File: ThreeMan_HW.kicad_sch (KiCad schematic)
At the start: 76 parts, among them J1 USB4135-GF-A, J2 JST-PH-2mm, J3 TC2030_ICSP, SW1 SW_Push, SW2 SW_SPDT_312, U1 MCP73831T-2ACI/OT, U2 74HC595, U3 ATTINY85-20SUR, U4 TPS7A20, U5 ULQ2003D, U6 ULQ2003D

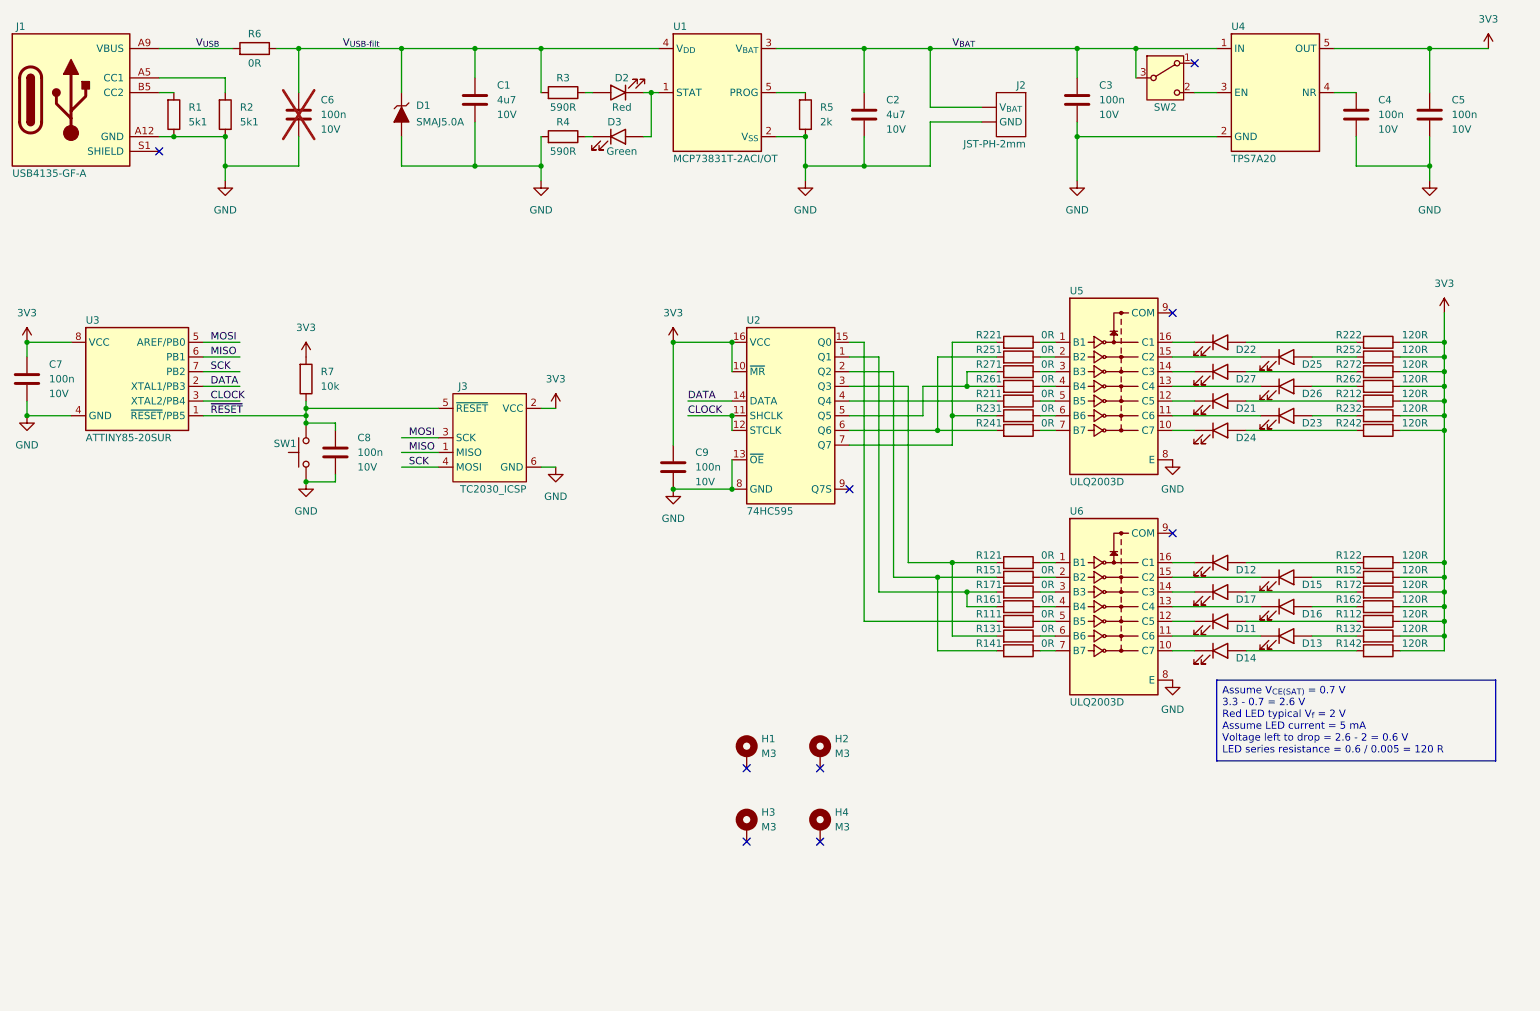
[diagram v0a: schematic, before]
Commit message: Ported all components to zpklib
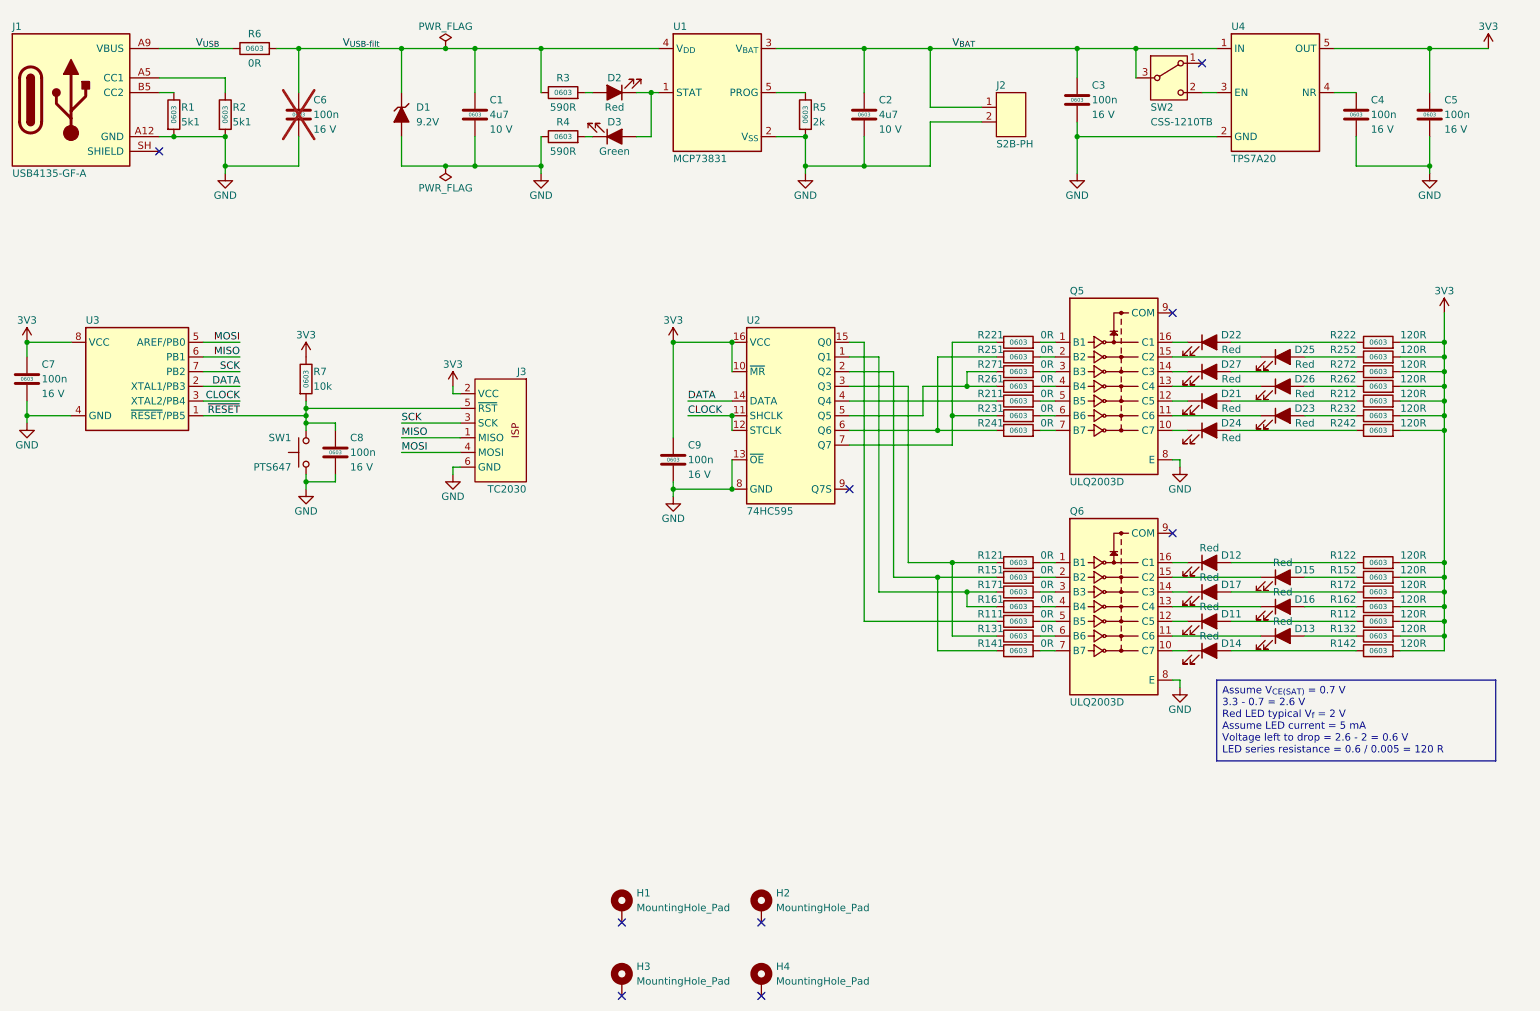
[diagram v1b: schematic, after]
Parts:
- removed J3: TC2030_ICSP, Connector:Tag-Connect_TC2030-IDC-FP_2x03_P1.27mm_Vertical, symbol Connector:Conn_TagConnect_TC2030_ICSP
- added J3: TC2030, connector_tagconnect:TagConnect_TC2030_2x3_DualSide, symbol connector_tagconnect:TC2030_ISP_DualSide
- C1, C2: footprint Capacitor_SMD:C_0603_HS -> capacitor:C_0603_1608Metric; symbol Capacitor:C_Generic -> zpklib:CC0603MRX5R6BB475; Case (none) -> 0603; Dielectric (none) -> X5R; IPN (none) -> C-00014; InvenTree (none) -> 106; MPN (none) -> CC0603MRX5R6BB475; Manufacturer (none) -> Yageo; MountingTypes (none) -> SMT; Package_Capacitor (none) -> capacitor:C_0603_1608Metric; Part URL (none) -> https://parts.b3rl1n.com/web/part/106/; TemperatureMax (none) -> 85 °C; TemperatureMin (none) -> -55 °C; Tolerance 10% -> 20 %; ValueStandard (none) -> 4.7u; Voltage 10V -> (none); VoltageRating (none) -> 10 V
- C3, C4, C5, C6, C7, C8, C9: footprint Capacitor_SMD:C_0603_HS -> capacitor:C_0603_1608Metric; symbol Capacitor:C_Generic -> zpklib:CC0603KRX7R7BB104; Case (none) -> 0603; Dielectric (none) -> X7R; IPN (none) -> C-00001; InvenTree (none) -> 24; MPN (none) -> CC0603KRX7R7BB104; Manufacturer (none) -> Yageo; MountingTypes (none) -> SMT; Package_Capacitor (none) -> capacitor:C_0603_1608Metric; Part URL (none) -> https://parts.b3rl1n.com/web/part/24/; TemperatureMax (none) -> 125 °C; TemperatureMin (none) -> -55 °C; Tolerance 10% -> 10 %; ValueStandard (none) -> 100n; Voltage 10V -> (none); VoltageRating (none) -> 16 V
- D1: value SMAJ5.0A -> 9.2V; footprint Diode_SMD:DO-214AC -> diode:D_SMA; symbol Diode_Zener:SMAJ5.0A-13-F -> zpklib:SMAJ5.0A; CurrentPeakPulse (none) -> 43.5 A; DK_PartNo SMAJ5.0ALFCT-ND -> (none); IPN (none) -> D-00007; InvenTree (none) -> 105; Manufacturer Littelfuse Inc. -> Littelfuse; MountingTypes (none) -> SMT; Package_Diode (none) -> diode:D_SMA; Part URL (none) -> https://parts.b3rl1n.com/web/part/105/; Symbol_Diode (none) -> diode:DiodeZener; TemperatureMax (none) -> 150 °C; TemperatureMin (none) -> -65 °C; ValueStandard (none) -> 9.2V; VoltageBreakdown (none) -> 6.4 V; VoltageClamping (none) -> 9.2 V; VoltageStandoff (none) -> 5 V
- D11, D12, D13, D14, D15, D16, D17, D2, D21, D22, D23, D24, D25, D26, D27: value Red -> LTST-C191KRKT; footprint LED_SMD:LED_0603_HS -> led:LED_0603_1608Metric; symbol LED:LED_Generic -> zpklib:LTST-C191KRKT; IPN (none) -> D-00005; InvenTree (none) -> 79; KicadHideFields (none) -> Value; LED_Colour (none) -> Red; MPN (none) -> LTST-C191KRKT; Manufacturer (none) -> LiteOn; MountingTypes (none) -> SMT; Package_LED (none) -> led:LED_0603_1608Metric; Part URL (none) -> https://parts.b3rl1n.com/web/part/79/; Symbol_LED (none) -> led:LED_x1; TemperatureMax (none) -> 85 °C; TemperatureMin (none) -> -55 °C; ValueStandard (none) -> LTST-C191KRKT; VoltageForward (none) -> 2 V
- D3: value Green -> LTST-C190KGKT[A; footprint LED_SMD:LED_0603_HS -> led:LED_0603_1608Metric; symbol LED:LED_Generic -> zpklib:LTST-C190KGKT; IPN (none) -> D-00004; InvenTree (none) -> 76; KicadHideFields (none) -> Value; LED_Colour (none) -> Green; MPN (none) -> LTST-C190KGKT[A; Manufacturer (none) -> LiteOn; MountingTypes (none) -> SMT; Package_LED (none) -> led:LED_0603_1608Metric; Part URL (none) -> https://parts.b3rl1n.com/web/part/76/; Symbol_LED (none) -> led:LED_x1; TemperatureMax (none) -> 85 °C; TemperatureMin (none) -> -30 °C; ValueStandard (none) -> LTST-C190KGKT[A; VoltageForward (none) -> 2.1 V
- H1, H2, H3, H4: value M3 -> MountingHole_Pad; footprint MountingHole:MountingHole_3.2mm_M3_Pad -> mounting_hole:MountingHole_3.2mm_Pad; symbol Mechanical:MountingHole_Pad_MP -> mounting_hole:MountingHole_Pad_M3
- J1: footprint Connector_USB:USB4135-GF-A -> connector_usb:GCT-USB4135-GF-A; symbol Connector_USB:USB4135-GF-A -> zpklib:USB4135-GF-A; ConnectorGender (none) -> Female; CurrentRating (none) -> 3 A; DK_PartNo 2073-USB4135-GF-A-ACT-ND -> (none); IPN (none) -> J-00010; InvenTree (none) -> 104; MountingTypes (none) -> SMT; Package_ConnectorUSB (none) -> connector_usb:GCT-USB4135-GF-A; Part URL (none) -> https://parts.b3rl1n.com/web/part/104/; Symbol_ConnectorUSB (none) -> connector:USB_C_Receptacle_PowerOnly; TemperatureMax (none) -> 85 °C; TemperatureMin (none) -> -30 °C; ValueStandard (none) -> USB4135-GF-A; VoltageRating (none) -> 48 V
- J2: value JST-PH-2mm -> S2B-PH; footprint Connector_JST:JST_PH_S2B-PH-SM4-TB_1x02-1MP_P2.00mm_Horizontal -> connector_jst:JST_PH_B2B-PH-SM4-TB_1x02-1MP_P2.00mm_Vertical; symbol Connector_JST:S2B-PH-SM4 -> zpklib:S2B-PH-SM4-TB; DK_PartNo 455-1749-1-ND -> (none); IPN (none) -> J-00011; InvenTree (none) -> 111; MountingTypes (none) -> SMT; NbrOfPositions (none) -> 2; Package_Connector (none) -> connector_jst:JST_PH_B2B-PH-SM4-TB_1x02-1MP_P2.00mm_Vertical; Part URL (none) -> https://parts.b3rl1n.com/web/part/111/; Symbol_Connector (none) -> connector:Conn_01x02; TemperatureMax (none) -> 85 °C; TemperatureMin (none) -> -25 °C; ValueStandard (none) -> S2B-PH
- Q5: renamed from U5; footprint Package_SO:SOIC-16-N_3.8x9.8mm_P1.27mm -> package_SO:SOIC-16_3.9x9.9mm_P1.27mm; symbol Transistor_Array:ULQ2003D -> zpklib:ULQ2003D1013TRY; CurrentRating (none) -> 500m A; DK_PartNo 497-10282-1-ND -> (none); IPN (none) -> Q-00002; InvenTree (none) -> 115; MountingTypes (none) -> SMT; Package_TransistorArray (none) -> package_SO:SOIC-16_3.9x9.9mm_P1.27mm; Part URL (none) -> https://parts.b3rl1n.com/web/part/115/; Symbol_TransistorArray (none) -> transistor_array:ULQ200X; TemperatureMax (none) -> 125 °C; TemperatureMin (none) -> -40 °C; TransistorType (none) -> NPN Darlington (BJT); ValueStandard (none) -> ULQ2003D; VoltageCollectorEmitter (none) -> 50 V
- Q6: renamed from U6; footprint Package_SO:SOIC-16-N_3.8x9.8mm_P1.27mm -> package_SO:SOIC-16_3.9x9.9mm_P1.27mm; symbol Transistor_Array:ULQ2003D -> zpklib:ULQ2003D1013TRY; CurrentRating (none) -> 500m A; DK_PartNo 497-10282-1-ND -> (none); IPN (none) -> Q-00002; InvenTree (none) -> 115; MountingTypes (none) -> SMT; Package_TransistorArray (none) -> package_SO:SOIC-16_3.9x9.9mm_P1.27mm; Part URL (none) -> https://parts.b3rl1n.com/web/part/115/; Symbol_TransistorArray (none) -> transistor_array:ULQ200X; TemperatureMax (none) -> 125 °C; TemperatureMin (none) -> -40 °C; TransistorType (none) -> NPN Darlington (BJT); ValueStandard (none) -> ULQ2003D; VoltageCollectorEmitter (none) -> 50 V
- R1, R2: footprint Resistor_SMD:R_0603_HS -> resistor:R_0603_1608Metric; symbol Resistor:R_Generic -> zpklib:RC0603FR-075K1L; Case (none) -> 0603; IPN (none) -> R-00014; InvenTree (none) -> 48; MPN (none) -> RC0603FR-075K1L; Manufacturer (none) -> Yageo; MountingTypes (none) -> SMT; Package_Resistor (none) -> resistor:R_0603_1608Metric; Part URL (none) -> https://parts.b3rl1n.com/web/part/48/; Power 0.125W -> 0.1 W; TemperatureMax (none) -> 155 °C; TemperatureMin (none) -> -55 °C; Tolerance 5% -> 1 %; ValueStandard (none) -> 5.1k
- R111, R121, R131, R141, R151, R161, R171, R211, R221, R231, R241, R251, R261, R271, R6: footprint Resistor_SMD:R_0603_HS -> resistor:R_0603_1608Metric; symbol Resistor:R_Generic -> zpklib:RC0603JR-070RL; Case (none) -> 0603; IPN (none) -> R-00016; InvenTree (none) -> 58; MPN (none) -> RC0603JR-070RL; Manufacturer (none) -> Yageo; MountingTypes (none) -> SMT; Package_Resistor (none) -> resistor:R_0603_1608Metric; Part URL (none) -> https://parts.b3rl1n.com/web/part/58/; Power 0.125W -> 0.1 W; TemperatureMax (none) -> 155 °C; TemperatureMin (none) -> -55 °C; Tolerance 5% -> %; ValueStandard (none) -> 0R
- R112, R122, R132, R142, R152, R162, R172, R212, R222, R232, R242, R252, R262, R272: footprint Resistor_SMD:R_0603_HS -> resistor:R_0603_1608Metric; symbol Resistor:R_Generic -> zpklib:RC0603FR-07120RL; Case (none) -> 0603; IPN (none) -> R-00028; InvenTree (none) -> 109; MPN (none) -> RC0603FR-07120RL; Manufacturer (none) -> Yageo; MountingTypes (none) -> SMT; Package_Resistor (none) -> resistor:R_0603_1608Metric; Part URL (none) -> https://parts.b3rl1n.com/web/part/109/; Power 0.125W -> 0.1 W; TemperatureMax (none) -> 155 °C; TemperatureMin (none) -> -55 °C; Tolerance 5% -> 1 %; ValueStandard (none) -> 120R
- R3, R4: footprint Resistor_SMD:R_0603_HS -> resistor:R_0603_1608Metric; symbol Resistor:R_Generic -> zpklib:RC0603FR-13590RL; Case (none) -> 0603; IPN (none) -> R-00026; InvenTree (none) -> 107; MPN (none) -> RC0603FR-13590RL; Manufacturer (none) -> Yageo; MountingTypes (none) -> SMT; Package_Resistor (none) -> resistor:R_0603_1608Metric; Part URL (none) -> https://parts.b3rl1n.com/web/part/107/; Power 0.125W -> 0.1 W; TemperatureMax (none) -> 155 °C; TemperatureMin (none) -> -55 °C; Tolerance 5% -> 1 %; ValueStandard (none) -> 590R
- R5: footprint Resistor_SMD:R_0603_HS -> resistor:R_0603_1608Metric; symbol Resistor:R_Generic -> zpklib:RC0603FR-102KL; Case (none) -> 0603; IPN (none) -> R-00027; InvenTree (none) -> 108; MPN (none) -> RC0603FR-102KL; Manufacturer (none) -> Yageo; MountingTypes (none) -> SMT; Package_Resistor (none) -> resistor:R_0603_1608Metric; Part URL (none) -> https://parts.b3rl1n.com/web/part/108/; Power 0.125W -> 0.1 W; TemperatureMax (none) -> 155 °C; TemperatureMin (none) -> -55 °C; Tolerance 5% -> 1 %; ValueStandard (none) -> 2k
- R7: footprint Resistor_SMD:R_0603_HS -> resistor:R_0603_1608Metric; symbol Resistor:R_Generic -> zpklib:RC0603FR-0710KL; Case (none) -> 0603; IPN (none) -> R-00002; InvenTree (none) -> 23; MPN (none) -> RC0603FR-0710KL; Manufacturer (none) -> Yageo; MountingTypes (none) -> SMT; Package_Resistor (none) -> resistor:R_0603_1608Metric; Part URL (none) -> https://parts.b3rl1n.com/web/part/23/; Power 0.125W -> 0.1 W; TemperatureMax (none) -> 155 °C; TemperatureMin (none) -> -55 °C; Tolerance 5% -> 1 %; ValueStandard (none) -> 10k
- SW1: value SW_Push -> PTS647; footprint Switch_Button_SMD:SW_SPST_TS04-66-95-BK-160-SMT -> switch:SW_Push_SPST_4.5x4.5mm_H7.0mm; symbol Switch_Button:TS04-66-95-BK-160-SMT -> zpklib:PTS647SM70SMTR2 LFS; ActuatorLength (none) -> 7 mm; ActuatorOperatingForce (none) -> 180 g; ActuatorOrientation (none) -> Top Actuated; CurrentRating (none) -> 50m A; DK_PartNo 2223-TS04-66-95-BK-160-SMT-ND -> (none); IPN (none) -> SW-00004; InvenTree (none) -> 117; MPN TS04-66-95-BK-160-SMT -> PTS647SM70SMTR2 LFS; Manufacturer (none) -> C&K; MountingTypes (none) -> SMT; Package_Switch (none) -> switch:SW_Push_SPST_4.5x4.5mm_H7.0mm; Part URL (none) -> https://parts.b3rl1n.com/web/part/117/; TemperatureMax (none) -> 85 °C; TemperatureMin (none) -> -40 °C; ValueStandard (none) -> PTS647; VoltageRating (none) -> 12 V
- SW2: value SW_SPDT_312 -> CSS-1210TB; footprint Switch_Slide_SMD:CSS-1210TB -> switch:CSS-1210TB; symbol Switch_Slide:CSS-1210TB -> zpklib:CSS-1210TB; ActuatorLength (none) -> 2 mm; ActuatorOperatingForce (none) -> 360 g; ActuatorOrientation (none) -> Side Actuated; ContactTiming (none) -> Non-shorting (BBM); CurrentRating (none) -> 100m A; DK_PartNo 563-1091-1-ND -> (none); IPN (none) -> SW-00003; InvenTree (none) -> 116; Manufacturer (none) -> Nidec Components; MountingTypes (none) -> SMT; Package_Switch (none) -> switch:CSS-1210TB; Part URL (none) -> https://parts.b3rl1n.com/web/part/116/; SwitchCircuit (none) -> SPDT; Symbol_Switch (none) -> switch:SW_SPDT_132; TemperatureMax (none) -> 70 °C; TemperatureMin (none) -> -20 °C; ValueStandard (none) -> CSS-1210TB; VoltageRating (none) -> 12 V
- U1: value MCP73831T-2ACI/OT -> MCP73831; footprint Package_TO_SOT_SMD:SOT-23-5 -> package_TO_SOT:SOT-23-5; symbol Battery_Charger:MCP73831T-2ACI/OT -> zpklib:MCP73831T-2ACI-OT; DK_PartNo MCP73831T-2ACI/OTCT-ND -> (none); IPN (none) -> U-00010; InvenTree (none) -> 110; MPN (none) -> MCP73831T-2ACI-OT; Manufacturer Microchip Technology -> Microship Technology; MountingTypes (none) -> SMT; Package_PowerManagement (none) -> package_TO_SOT:SOT-23-5; Part URL (none) -> https://parts.b3rl1n.com/web/part/110/; Symbol_PowerManagement (none) -> power_management:MCP7383X; TemperatureMax (none) -> 85 °C; TemperatureMin (none) -> -40 °C; ValueStandard (none) -> MCP73831
- U2: footprint Package_SO:TSSOP-16_4.4x5mm_P0.65mm -> package_SO:TSSOP-16_4.4x5mm_P0.65mm; symbol Interface_ShiftRegister:74HC595PW,118 -> zpklib:74HC595PW,118; DK_PartNo 1727-3068-1-ND -> (none); IPN (none) -> U-00013; InvenTree (none) -> 114; MPN (none) -> 74HC595PW,118; Manufacturer Nexperia USA Inc. -> Nexperia; MountingTypes (none) -> SMT; Package_InterfaceShiftRegister (none) -> package_SO:TSSOP-16_4.4x5mm_P0.65mm; Part URL (none) -> https://parts.b3rl1n.com/web/part/114/; Symbol_InterfaceShiftRegister (none) -> interface_shiftregister:74HC595; TemperatureMax (none) -> 125 °C; TemperatureMin (none) -> -40 °C; ValueStandard (none) -> 74HC595
- U3: value ATTINY85-20SUR -> ATTINY85; footprint Package_SO:SOIC-8_5.3x5.3mm_P1.27mm -> package_SO:SOIC-8_5.3x5.3mm_P1.27mm; symbol MCU_Microchip_ATtiny:ATTINY85-20SUR -> zpklib:ATTINY85-20SUR; DK_PartNo ATTINY85-20SURCT-ND -> (none); IPN (none) -> U-00012; InvenTree (none) -> 113; KicadHideFields (none) -> Value; MCU_NbrIO (none) -> 6; MCU_SizeCore (none) -> 8-bit; MCU_SizeFlash (none) -> 8k B; MCU_SizeRAM (none) -> 4k B; MCU_Speed (none) -> 20M Hz; MPN (none) -> ATTINY85-20SUR; MountingTypes (none) -> SMT; Package_Microcontroller (none) -> package_SO:SOIC-8_5.3x5.3mm_P1.27mm; Part URL (none) -> https://parts.b3rl1n.com/web/part/113/; Symbol_Microcontroller-Atmel (none) -> microcontroller_atmel:ATTINY25-45-85; TemperatureMax (none) -> 85 °C; TemperatureMin (none) -> -40 °C; ValueStandard (none) -> ATTINY85
- U4: footprint Package_TO_SOT_SMD:SOT-23-5 -> package_TO_SOT:SOT-23-5; symbol Regulator_Linear:TPS7A20 -> zpklib:TPS7A2033PDBVR; Channels (none) -> 1; CurrentOutput (none) -> 300m A; DK_PartNo 296-TPS7A2033PDBVRCT-ND -> (none); IPN (none) -> U-00011; InvenTree (none) -> 112; MountingTypes (none) -> SMT; Package_RegulatorLinear (none) -> package_TO_SOT:SOT-23-5; Part URL (none) -> https://parts.b3rl1n.com/web/part/112/; Symbol_RegulatorLinear (none) -> regulator_linear:TPS7A20; TemperatureMax (none) -> 125 °C; TemperatureMin (none) -> -40 °C; ValueStandard (none) -> TPS7A20
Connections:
- net 3V3: now also J3.2 (VCC)
- net GND: now also J3.6 (GND)
- net MISO: now also J3.1 (MISO)
- net MOSI: now also J3.4 (MOSI)
- net SCK: now also J3.3 (SCK)
- net ~{RESET}: now also J3.5 (~{RST})
- net at R272.1: now also D27.A; no longer D27.1 (A)
- net at Q5.14 (C3): now also D27.C; no longer D27.2 (K)
- net at R142.1: now also D14.A; no longer D14.1 (A)
- net at R262.1: now also D26.A; no longer D26.1 (A)
- net at Q5.13 (C4): now also D26.C; no longer D26.2 (K)
- net at R4.2: now also D3.C; no longer D3.2 (K)
- net at R112.1: now also D11.A; no longer D11.1 (A)
- net at R212.1: now also D21.A; no longer D21.1 (A)
- net at Q5.12 (C5): now also D21.C; no longer D21.2 (K)
- net at R242.1: now also D24.A; no longer D24.1 (A)
- net at R122.1: now also D12.A; no longer D12.1 (A)
- net at R162.1: now also D16.A; no longer D16.1 (A)
- net at R232.1: now also D23.A; no longer D23.1 (A)
- net at R222.1: now also D22.A; no longer D22.1 (A)
- net at Q5.16 (C1): now also D22.C; no longer D22.2 (K)
- net at R152.1: now also D15.A; no longer D15.1 (A)
- net at Q6.15 (C2): now also D15.C; no longer D15.2 (K)
- net at R132.1: now also D13.A; no longer D13.1 (A)
- net at R252.1: now also D25.A; no longer D25.1 (A)
- net at Q5.15 (C2): now also D25.C; no longer D25.2 (K)
- net at Q5.10 (C7): now also D24.C; no longer D24.2 (K)
- net at Q6.13 (C4): now also D16.C; no longer D16.2 (K)
- net at R172.1: now also D17.A; no longer D17.1 (A)
- net at R3.2: now also D2.A; no longer D2.1 (A)
- net at Q5.11 (C6): now also D23.C; no longer D23.2 (K)
- net at Q6.14 (C3): now also D17.C; no longer D17.2 (K)
- net at Q6.11 (C6): now also D13.C; no longer D13.2 (K)
- net at Q6.10 (C7): now also D14.C; no longer D14.2 (K)
- net at Q6.12 (C5): now also D11.C; no longer D11.2 (K)
- net at Q6.16 (C1): now also D12.C; no longer D12.2 (K)
- new net: D2.C, D3.A, U1.1 (STAT)
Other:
- company: Zkylark Electronics -> ${COMPANY}
- title: ThreeMan -> ${PROJECT_NAME}
- moved on the sheet: C1, C9, D1, H1, H2, H3, H4, SW2
